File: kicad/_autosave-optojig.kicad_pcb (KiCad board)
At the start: 2 copper layers, 200 x 100 mm, 19 parts, among them Q1 2N2219, Q2 2N2219, SW1 Switch_SPDT_x2, U1 TRN1-0510, U2 LM358

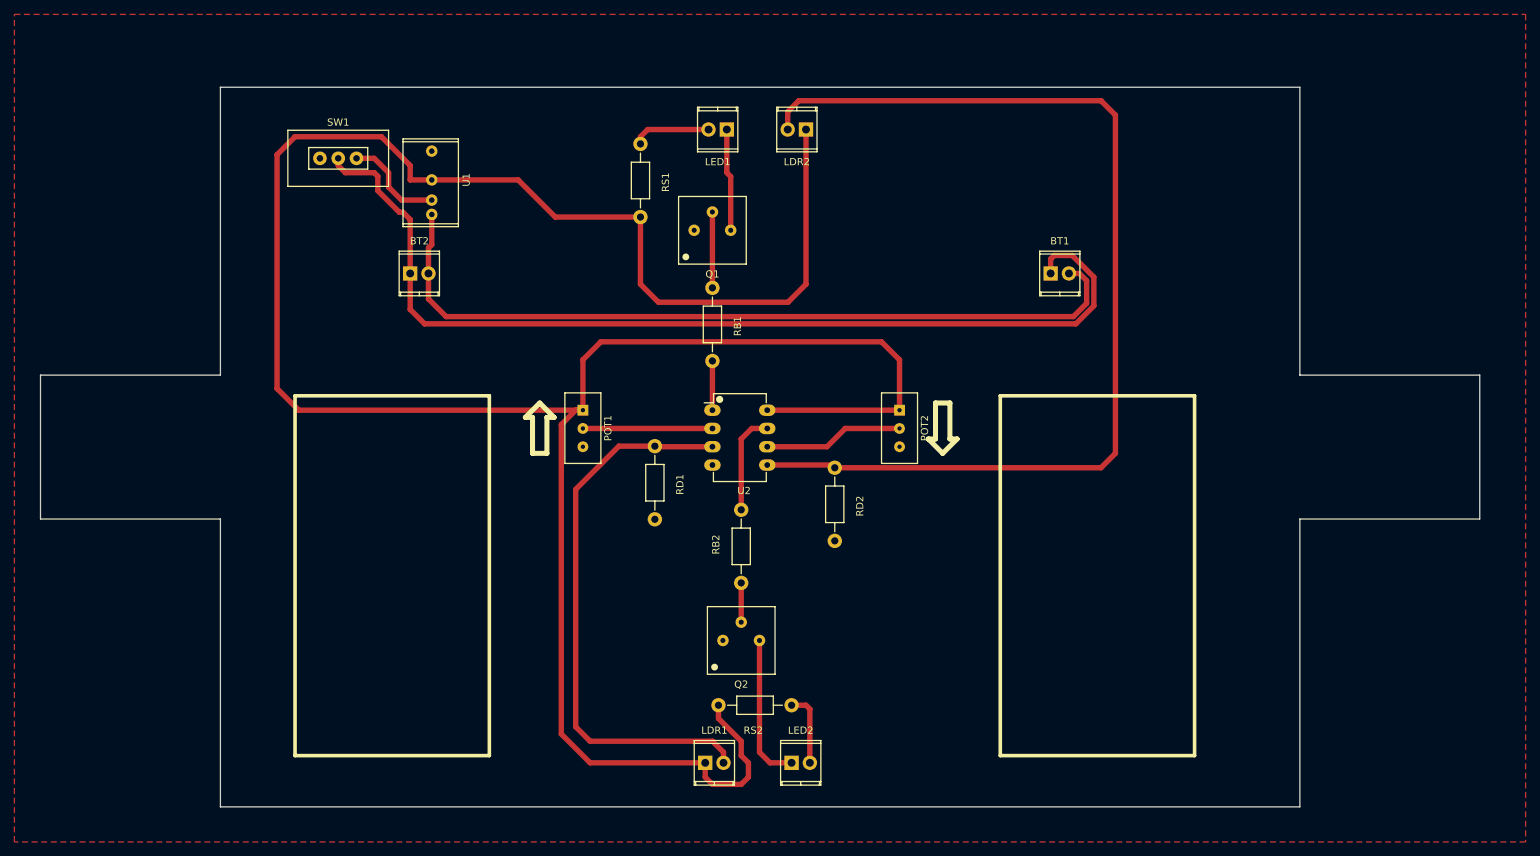
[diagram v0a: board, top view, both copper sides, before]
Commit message: Added battery holder datasheet
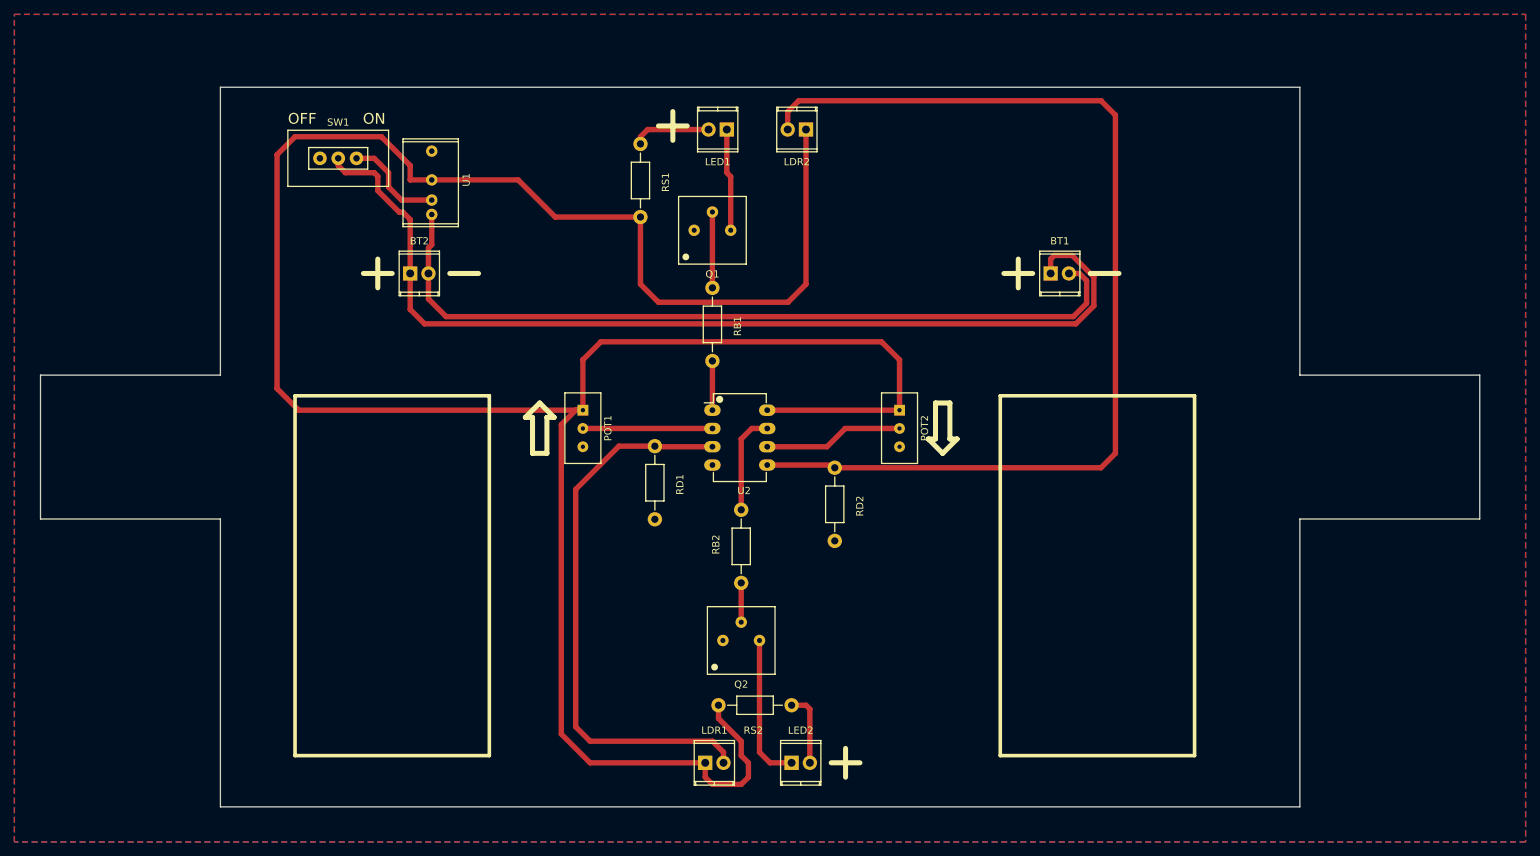
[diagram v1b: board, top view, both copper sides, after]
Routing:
- added copper zone on B.Cu, net GND
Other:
- board text added: "OFF"
- board text added: "ON"
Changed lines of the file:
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@@
     (links 33)
     (no_connects 0)
-    (area 43.578599 45.073899 243.678601 145.173901)
+    (area 40 35 250.000001 150.000001)
     (thickness 1.6)
-    (drawings 34)
+    (drawings 46)
     (tracks 109)
     (zones 0)
@@
   (page A4)
   (layers
-    (0 F.Cu signal)
+    (0 F.Cu signal hide)
     (31 B.Cu signal)
-    (32 B.Adhes user)
-    (33 F.Adhes user)
-    (34 B.Paste user)
-    (35 F.Paste user)
-    (36 B.SilkS user)
-    (37 F.SilkS user)
-    (38 B.Mask user)
-    (39 F.Mask user)
-    (40 Dwgs.User user)
-    (41 Cmts.User user)
-    (42 Eco1.User user)
-    (43 Eco2.User user)
-    (44 Edge.Cuts user)
-    (45 Margin user)
-    (46 B.CrtYd user)
-    (47 F.CrtYd user)
-    (48 B.Fab user)
-    (49 F.Fab user)
+    (32 B.Adhes user hide)
+    (33 F.Adhes user hide)
+    (34 B.Paste user hide)
+    (35 F.Paste user hide)
+    (36 B.SilkS user hide)
+    (37 F.SilkS user hide)
+    (38 B.Mask user hide)
+    (39 F.Mask user hide)
+    (40 Dwgs.User user hide)
+    (41 Cmts.User user hide)
+    (42 Eco1.User user hide)
+    (43 Eco2.User user hide)
+    (44 Edge.Cuts user hide)
+    (45 Margin user hide)
+    (46 B.CrtYd user hide)
+    (47 F.CrtYd user hide)
+    (48 B.Fab user hide)
+    (49 F.Fab user hide)
   )
   (setup
@@
     (visible_elements FFFFFF7F)
     (pcbplotparams
-      (layerselection 0x00030_80000001)
+      (layerselection 0x010e0_80000001)
       (usegerberextensions false)
       (excludeedgelayer true)
@@
       (outputformat 1)
       (mirror false)
-      (drillshape 1)
+      (drillshape 0)
       (scaleselection 1)
-      (outputdirectory ""))
+      (outputdirectory gerber/))
   )
   (net 0 "")
@@
       (net 6 "Net-(SW1-Pad3)"))
   )
+  (gr_line (start 131.5 48.5) (end 131.5 52.5) (angle 90) (layer F.SilkS) (width 0.7))
+  (gr_line (start 129.5 50.5) (end 133.5 50.5) (angle 90) (layer F.SilkS) (width 0.7))
+  (gr_line (start 155.5 137) (end 155.5 141) (angle 90) (layer F.SilkS) (width 0.7))
+  (gr_line (start 153.5 139) (end 157.5 139) (angle 90) (layer F.SilkS) (width 0.7))
+  (gr_line (start 189.5 71) (end 193.5 71) (angle 90) (layer F.SilkS) (width 0.7))
+  (gr_line (start 177.5 71) (end 181.5 71) (angle 90) (layer F.SilkS) (width 0.7))
+  (gr_line (start 179.5 69) (end 179.5 73) (angle 90) (layer F.SilkS) (width 0.7))
+  (gr_line (start 100.5 71) (end 104.5 71) (angle 90) (layer F.SilkS) (width 0.7))
+  (gr_line (start 90.5 69) (end 90.5 73) (angle 90) (layer F.SilkS) (width 0.7))
+  (gr_line (start 88.5 71) (end 92.5 71) (angle 90) (layer F.SilkS) (width 0.7))
+  (gr_text OFF (at 80 49.5) (layer F.SilkS)
+    (effects (font (size 1.5 1.5) (thickness 0.3)))
+  )
+  (gr_text ON (at 90 49.5) (layer F.SilkS)
+    (effects (font (size 1.5 1.5) (thickness 0.3)))
+  )
   (gr_line (start 170 89) (end 168 89) (angle 90) (layer F.SilkS) (width 0.7))
   (gr_line (start 168 89) (end 168 94) (angle 90) (layer F.SilkS) (width 0.7))
@@
   (segment (start 98 67) (end 98 62.8) (width 0.75) (layer F.Cu) (net 1))
   (segment (start 97.54 67.46) (end 98 67) (width 0.75) (layer F.Cu) (net 1))
-  (segment (start 85 55) (end 85 56) (width 0.75) (layer F.Cu) (net 2) (status 400000))
-  (segment (start 95 63.5) (end 95 71) (width 0.75) (layer F.Cu) (net 2) (status 800000))
+  (segment (start 85 55) (end 85 56) (width 0.75) (layer F.Cu) (net 2))
+  (segment (start 95 63.5) (end 95 71) (width 0.75) (layer F.Cu) (net 2))
   (segment (start 94 62.5) (end 95 63.5) (width 0.75) (layer F.Cu) (net 2))
   (segment (start 93.5 62.5) (end 94 62.5) (width 0.75) (layer F.Cu) (net 2))
@@
   (segment (start 86 57) (end 90 57) (width 0.75) (layer F.Cu) (net 2))
   (segment (start 85 56) (end 86 57) (width 0.75) (layer F.Cu) (net 2))
-  (segment (start 95 71) (end 95 76) (width 0.75) (layer F.Cu) (net 2) (status 400000))
+  (segment (start 95 71) (end 95 76) (width 0.75) (layer F.Cu) (net 2))
   (segment (start 95 76) (end 97 78) (width 0.75) (layer F.Cu) (net 2))
   (segment (start 97 78) (end 187.5 78) (width 0.75) (layer F.Cu) (net 2))
@@
   (segment (start 187 68.5) (end 184.5 68.5) (width 0.75) (layer F.Cu) (net 2))
   (segment (start 184.5 68.5) (end 184 69) (width 0.75) (layer F.Cu) (net 2))
-  (segment (start 184 69) (end 184 71) (width 0.75) (layer F.Cu) (net 2) (status 800000))
+  (segment (start 184 69) (end 184 71) (width 0.75) (layer F.Cu) (net 2))
   (segment (start 137 73) (end 137 62.46) (width 0.75) (layer F.Cu) (net 3))
   (segment (start 141 114) (end 141 119.46) (width 0.75) (layer F.Cu) (net 4))
@@
   (segment (start 137 95.08) (end 129.08 95.08) (width 0.75) (layer F.Cu) (net 8))
   (segment (start 129.08 95.08) (end 129 95) (width 0.75) (layer F.Cu) (net 8))
+  (segment (start 163 90) (end 144.62 90) (width 0.75) (layer F.Cu) (net 9))
   (segment (start 98 58) (end 95 58) (width 0.75) (layer F.Cu) (net 9))
   (segment (start 79.5 90) (end 119 90) (width 0.75) (layer F.Cu) (net 9))
@@
   (segment (start 115.16 63.16) (end 127 63.16) (width 0.75) (layer F.Cu) (net 9))
   (segment (start 110 58) (end 115.16 63.16) (width 0.75) (layer F.Cu) (net 9))
-  (segment (start 163 90) (end 144.62 90) (width 0.75) (layer F.Cu) (net 9))
   (segment (start 154 98) (end 191 98) (width 0.75) (layer F.Cu) (net 10))
   (segment (start 147.46 48.54) (end 147.46 51) (width 0.75) (layer F.Cu) (net 10))
@@
   (segment (start 193 96) (end 193 49) (width 0.75) (layer F.Cu) (net 10))
   (segment (start 191 98) (end 193 96) (width 0.75) (layer F.Cu) (net 10))
+  (segment (start 153.62 97.62) (end 154 98) (width 0.75) (layer F.Cu) (net 10))
   (segment (start 144.62 97.62) (end 153.62 97.62) (width 0.75) (layer F.Cu) (net 10))
-  (segment (start 153.62 97.62) (end 154 98) (width 0.75) (layer F.Cu) (net 10))
   (segment (start 136.46 51) (end 128 51) (width 0.75) (layer F.Cu) (net 11))
   (segment (start 127 52) (end 127 53) (width 0.75) (layer F.Cu) (net 11))
@@
   (segment (start 143.54 137.54) (end 145 139) (width 0.75) (layer F.Cu) (net 14))
   (segment (start 137 92.54) (end 119 92.54) (width 0.75) (layer F.Cu) (net 15))
+  (segment (start 152.92 95.08) (end 144.62 95.08) (width 0.75) (layer F.Cu) (net 16))
   (segment (start 163 92.54) (end 155.46 92.54) (width 0.75) (layer F.Cu) (net 16))
-  (segment (start 152.92 95.08) (end 144.62 95.08) (width 0.75) (layer F.Cu) (net 16))
   (segment (start 155.46 92.54) (end 152.92 95.08) (width 0.75) (layer F.Cu) (net 16))
   (segment (start 137 83.16) (end 137 90) (width 0.75) (layer F.Cu) (net 17))
+  (segment (start 142.46 92.54) (end 144.62 92.54) (width 0.75) (layer F.Cu) (net 18))
   (segment (start 141 103.84) (end 141 94) (width 0.75) (layer F.Cu) (net 18))
-  (segment (start 142.46 92.54) (end 144.62 92.54) (width 0.75) (layer F.Cu) (net 18))
   (segment (start 141 94) (end 142.46 92.54) (width 0.75) (layer F.Cu) (net 18))
   (zone (net 7) (net_name GND) (layer F.Cu) (hatch edge 0.508)
     (connect_pads (clearance 0.25))
     (min_thickness 0.254)
+    (fill yes (arc_segments 16) (thermal_gap 0.508) (thermal_bridge_width 3))
+    (polygon
+      (pts
+        (xy 250 150) (xy 40 150) (xy 40 35) (xy 250 35) (xy 250 150)
+      )
+    )
+  )
+  (zone (net 7) (net_name GND) (layer B.Cu) (hatch edge 0.508)
+    (connect_pads (clearance 0.25))
+    (min_thickness 0.254)

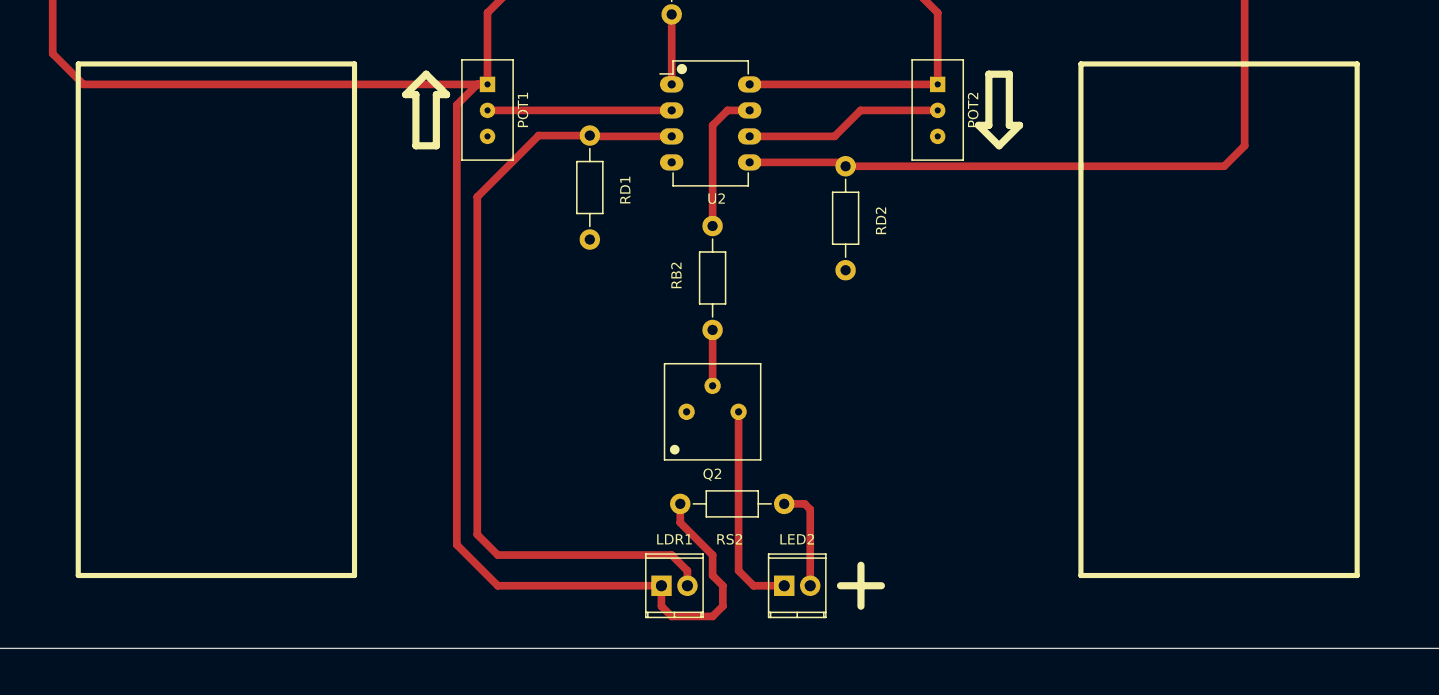
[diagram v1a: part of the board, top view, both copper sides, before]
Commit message: Added gerber files zip
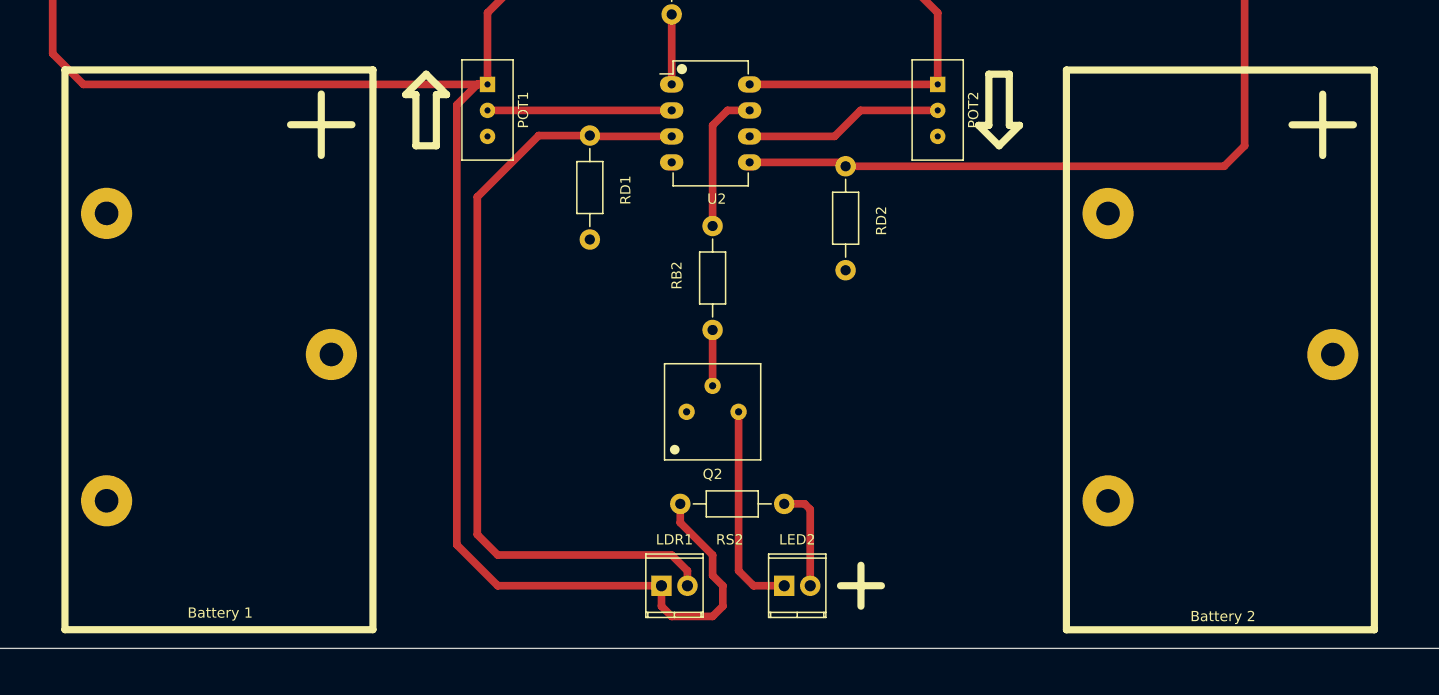
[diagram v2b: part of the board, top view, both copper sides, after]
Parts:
- added Battery 1: Batt_hold, optojig-footprints:Batt_hold, F.Cu at (92.8, 115.9)
- added Battery 2: Batt_hold, optojig-footprints:Batt_hold, F.Cu at (190.6, 116.0)
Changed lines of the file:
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@@
     (area 40 35 250.000001 150.000001)
     (thickness 1.6)
-    (drawings 46)
+    (drawings 38)
     (tracks 109)
     (zones 0)
-    (modules 19)
+    (modules 21)
     (nets 19)
   )
   (page A4)
   (layers
-    (0 F.Cu signal hide)
-    (31 B.Cu signal)
+    (0 F.Cu signal)
+    (31 B.Cu signal hide)
     (32 B.Adhes user hide)
     (33 F.Adhes user hide)
@@
     (35 F.Paste user hide)
     (36 B.SilkS user hide)
-    (37 F.SilkS user hide)
+    (37 F.SilkS user)
     (38 B.Mask user hide)
     (39 F.Mask user hide)
@@
     (add_net "Net-(SW1-Pad3)")
   )
+  (module optojig-footprints:Batt_hold (layer F.Cu)
+    (at 190.63 115.95)
+    (fp_text reference "Battery 2" (at 0.25 26.05) (layer F.SilkS)
+      (effects (font (size 1 1) (thickness 0.15)))
+    )
+    (fp_text value Batt_hold (at 0 -29) (layer F.Fab)
+      (effects (font (size 1 1) (thickness 0.15)))
+    )
+    (fp_line (start 10 -25) (end 10 -19) (layer F.SilkS) (width 0.7))
+    (fp_line (start 7 -22) (end 13 -22) (layer F.SilkS) (width 0.7))
+    (fp_line (start -15.05 -27.355) (end 15.05 -27.355) (layer F.SilkS) (width 0.7))
+    (fp_line (start -15.05 27.355) (end 15.05 27.355) (layer F.SilkS) (width 0.7))
+    (fp_line (start 15.05 -27.355) (end 15.05 27.355) (layer F.SilkS) (width 0.7))
+    (fp_line (start -15.05 -27.355) (end -15.05 27.355) (layer F.SilkS) (width 0.7))
+    (pad GND thru_hole circle (at -10.98 -13.335) (size 5 5) (drill 2.31) (layers *.Cu *.Mask F.SilkS))
+    (pad GND thru_hole circle (at 10.99 0.455) (size 5 5) (drill 2.31) (layers *.Cu *.Mask F.SilkS))
+    (pad GND thru_hole circle (at -10.98 14.755) (size 5 5) (drill 2.31) (layers *.Cu *.Mask F.SilkS))
+  )
   (module optojig-footprints:TerminalBlock_Buchanan_2way (layer F.Cu)
     (at 184 71)
@@
       (net 6 "Net-(SW1-Pad3)"))
   )
+  (module optojig-footprints:Batt_hold (layer F.Cu)
+    (at 92.75 115.94)
+    (fp_text reference "Battery 1" (at 0.12 25.72) (layer F.SilkS)
+      (effects (font (size 1 1) (thickness 0.15)))
+    )
+    (fp_text value Batt_hold (at 0 -29) (layer F.Fab)
+      (effects (font (size 1 1) (thickness 0.15)))
+    )
+    (fp_line (start 10 -25) (end 10 -19) (layer F.SilkS) (width 0.7))
+    (fp_line (start 7 -22) (end 13 -22) (layer F.SilkS) (width 0.7))
+    (fp_line (start -15.05 -27.355) (end 15.05 -27.355) (layer F.SilkS) (width 0.7))
+    (fp_line (start -15.05 27.355) (end 15.05 27.355) (layer F.SilkS) (width 0.7))
+    (fp_line (start 15.05 -27.355) (end 15.05 27.355) (layer F.SilkS) (width 0.7))
+    (fp_line (start -15.05 -27.355) (end -15.05 27.355) (layer F.SilkS) (width 0.7))
+    (pad GND thru_hole circle (at -10.98 -13.335) (size 5 5) (drill 2.31) (layers *.Cu *.Mask F.SilkS))
+    (pad GND thru_hole circle (at 10.99 0.455) (size 5 5) (drill 2.31) (layers *.Cu *.Mask F.SilkS))
+    (pad GND thru_hole circle (at -10.98 14.755) (size 5 5) (drill 2.31) (layers *.Cu *.Mask F.SilkS))
+  )
   (gr_line (start 131.5 48.5) (end 131.5 52.5) (angle 90) (layer F.SilkS) (width 0.7))
   (gr_line (start 129.5 50.5) (end 133.5 50.5) (angle 90) (layer F.SilkS) (width 0.7))
@@
   (gr_line (start 114 96) (end 114 91) (angle 90) (layer F.SilkS) (width 0.7))
   (gr_line (start 112 96) (end 114 96) (angle 90) (layer F.SilkS) (width 0.7))
-  (gr_line (start 79 88) (end 106 88) (angle 90) (layer F.SilkS) (width 0.5))
-  (gr_line (start 79 138) (end 106 138) (angle 90) (layer F.SilkS) (width 0.5))
-  (gr_line (start 79 88) (end 79 138) (angle 90) (layer F.SilkS) (width 0.5))
-  (gr_line (start 106 138) (end 106 88) (angle 90) (layer F.SilkS) (width 0.5))
-  (gr_line (start 204 138) (end 204 88) (angle 90) (layer F.SilkS) (width 0.5))
-  (gr_line (start 177 88) (end 177 138) (angle 90) (layer F.SilkS) (width 0.5))
-  (gr_line (start 177 138) (end 204 138) (angle 90) (layer F.SilkS) (width 0.5))
-  (gr_line (start 177 88) (end 204 88) (angle 90) (layer F.SilkS) (width 0.5))
   (gr_line (start 68.6286 85.1239) (end 68.6286 45.1239) (layer Edge.Cuts) (width 0.1))
   (gr_line (start 43.6286 85.1239) (end 68.6286 85.1239) (layer Edge.Cuts) (width 0.1))
